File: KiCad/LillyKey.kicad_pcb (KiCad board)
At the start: 2 copper layers, 140 x 92 mm, 66 parts, among them J1 Conn_01x02_Socket, SW1 SW_Push, SW10 SW_Push, SW11 SW_Push, SW12 SW_Push, SW13 SW_Push, SW14 SW_Push, SW15 SW_Push, SW16 SW_Push, SW17 SW_Push, SW18 SW_Push, SW19 SW_Push, SW2 SW_Push, SW20 SW_Push, SW21 SW_Push, SW22 SW_Push, SW23 SW_Push, SW24 SW_Push, SW25 SW_Push, SW26 SW_Push, SW27 SW_Push, SW28 SW_Push, SW29 SW_Push, SW3 SW_Push, SW30 SW_Push, SW4 SW_Push, SW5 SW_Push, SW6 SW_Push, SW7 SW_Push, SW8 SW_Push, SW9 SW_Push, U2 XIAO-nRF52840-SMD

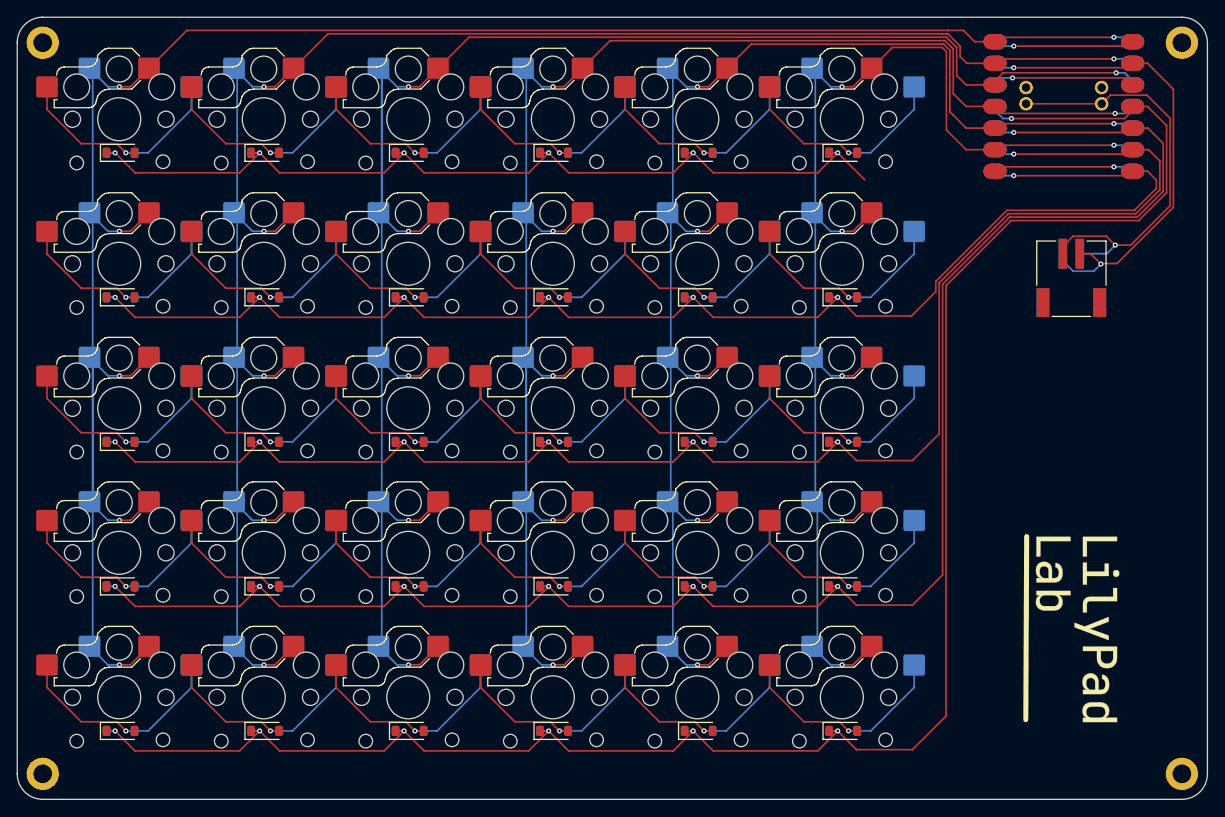
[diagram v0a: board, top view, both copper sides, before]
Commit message: Fliped around keys, cleanup
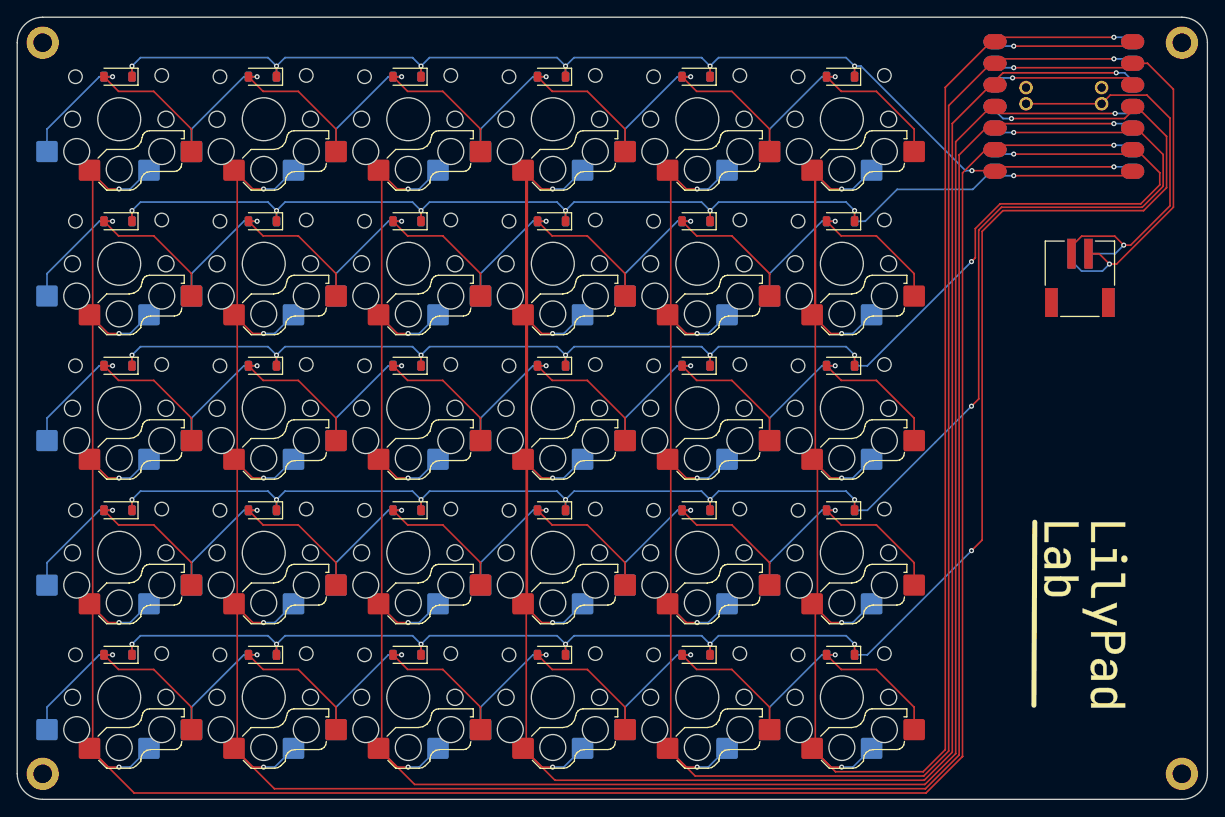
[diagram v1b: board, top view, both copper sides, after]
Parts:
- D1, D10, D11, D12, D13, D14, D15, D16, D17, D18, D19, D2, D20, D21, D22, D23, D24, D25, D26, D27, D28, D29, D3, D30, D4, D5, D6, D7, D8, D9: footprint ExtraFootprints:RevDiode -> Footprints:RevDiode; moved to F.Cu
- J1: footprint ExtraFootprints:JSTPH -> Footprints:JSTPH
- SW1, SW10, SW11, SW12, SW13, SW14, SW15, SW16, SW17, SW18, SW19, SW2, SW20, SW21, SW22, SW23, SW24, SW25, SW26, SW27, SW28, SW29, SW3, SW30, SW4, SW5, SW6, SW7, SW8, SW9: footprint ExtraFootprints:SW_Hotswap_Kailh_Choc_V1V2 -> Footprints:SW_Hotswap_Kailh_Choc_V1V2
- U2: footprint ExtraFootprints:XIAO_nRF52840_DUAL -> Footprints:XIAO_nRF52840_DUAL
- moved D1 8.95 mm to (34.0, 29.0), turned to 180 degrees
- moved D10 8.95 mm to (85.0, 46.0), turned to 180 degrees
- moved D11 8.95 mm to (102.0, 46.0), turned to 180 degrees
- moved D12 8.95 mm to (119.0, 46.0), turned to 180 degrees
- moved D13 8.95 mm to (34.0, 63.0), turned to 180 degrees
- moved D14 8.95 mm to (51.0, 63.0), turned to 180 degrees
- moved D15 8.95 mm to (68.0, 63.0), turned to 180 degrees
- moved D16 8.95 mm to (85.0, 63.0), turned to 180 degrees
- moved D17 8.95 mm to (102.0, 63.0), turned to 180 degrees
- moved D18 8.95 mm to (119.0, 63.0), turned to 180 degrees
- moved D19 8.95 mm to (34.0, 80.0), turned to 180 degrees
- moved D2 8.95 mm to (51.0, 29.0), turned to 180 degrees
- moved D20 8.95 mm to (51.0, 80.0), turned to 180 degrees
- moved D21 8.95 mm to (68.0, 80.0), turned to 180 degrees
- moved D22 8.95 mm to (85.0, 80.0), turned to 180 degrees
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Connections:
- U2 pad 1: /COL0 -> /COL5
- U2 pad 2: /COL1 -> /COL4
- U2 pad 3: /COL2 -> /COL3
- U2 pad 4: /COL3 -> /COL2
- U2 pad 5: /COL4 -> /COL1
- U2 pad 6: /COL5 -> /COL0
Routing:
- net /COL3: track 203.2 -> 366.5 mm
- net /COL5: track 156.5 -> 251.0 mm
- net /COL1: track 216.7 -> 295.5 mm
- net /COL4: track 171.8 -> 249.5 mm
- net /COL2: track 218.8 -> 283.7 mm
- net /COL0: track 248.7 -> 310.7 mm
- net /ROW1: track 173.5 -> 140.6 mm
- net /ROW2: track 193.5 -> 173.7 mm, vias 7 -> 8
- net /ROW3: track 213.4 -> 193.6 mm, vias 7 -> 8
- net /ROW4: track 233.9 -> 214.2 mm, vias 7 -> 8
- net /ROW0: track 129.0 -> 142.9 mm, vias 7 -> 8
- net Net-(D9-A): track 27.5 -> 29.4 mm
- net Net-(D8-A): track 27.5 -> 29.4 mm
- net Net-(D7-A): track 27.5 -> 29.4 mm
- net Net-(D28-A): track 27.5 -> 29.4 mm
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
